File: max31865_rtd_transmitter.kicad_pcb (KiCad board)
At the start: 2 copper layers, 11 parts, among them CN1 WJ15EDGRM-3.81-4P-14-00A, SW1 MST22D18G2, T1 VPT87BB-01B, U1 MAX31865xTP, U2 VPS8504B, U3 TPS7A2033PDBVR, U4 TPS7A2033PDBVR, U5 ISO7741DWR

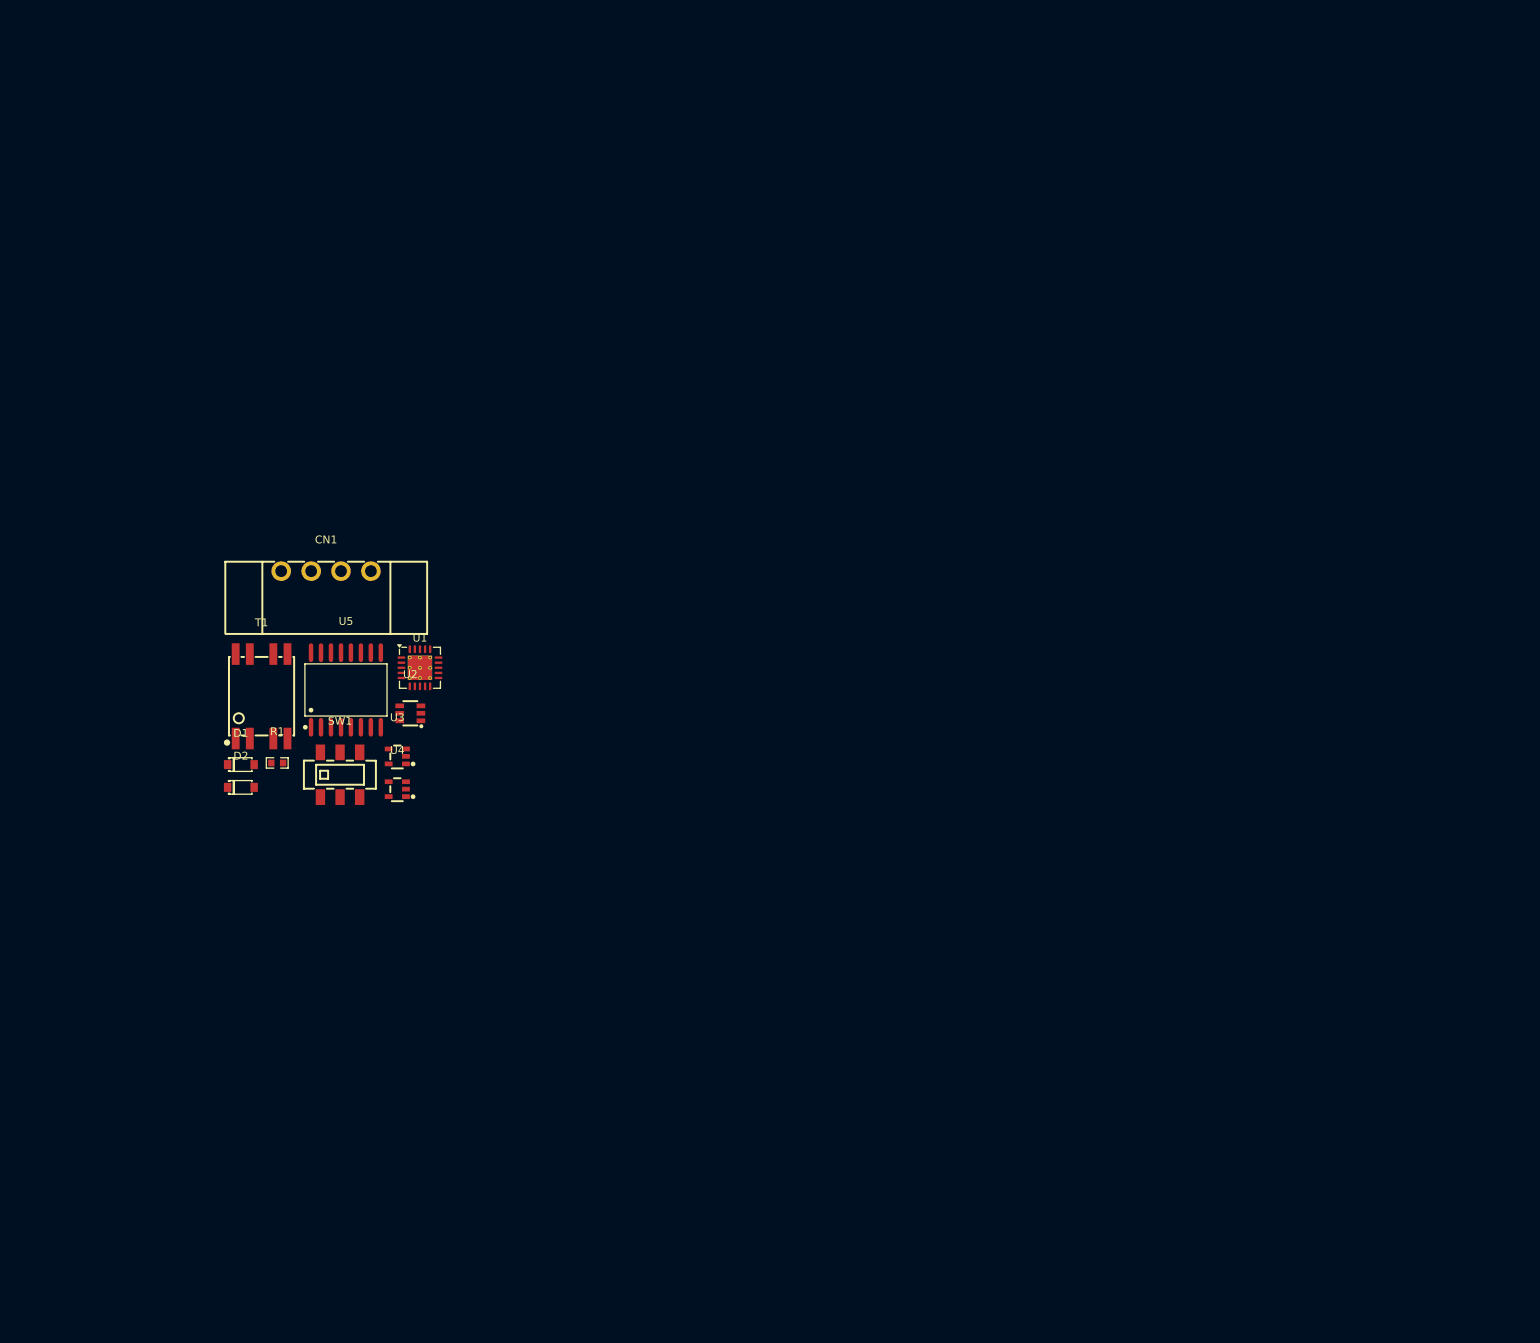
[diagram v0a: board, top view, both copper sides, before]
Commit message: Complete max31865 power supply and analog component layout
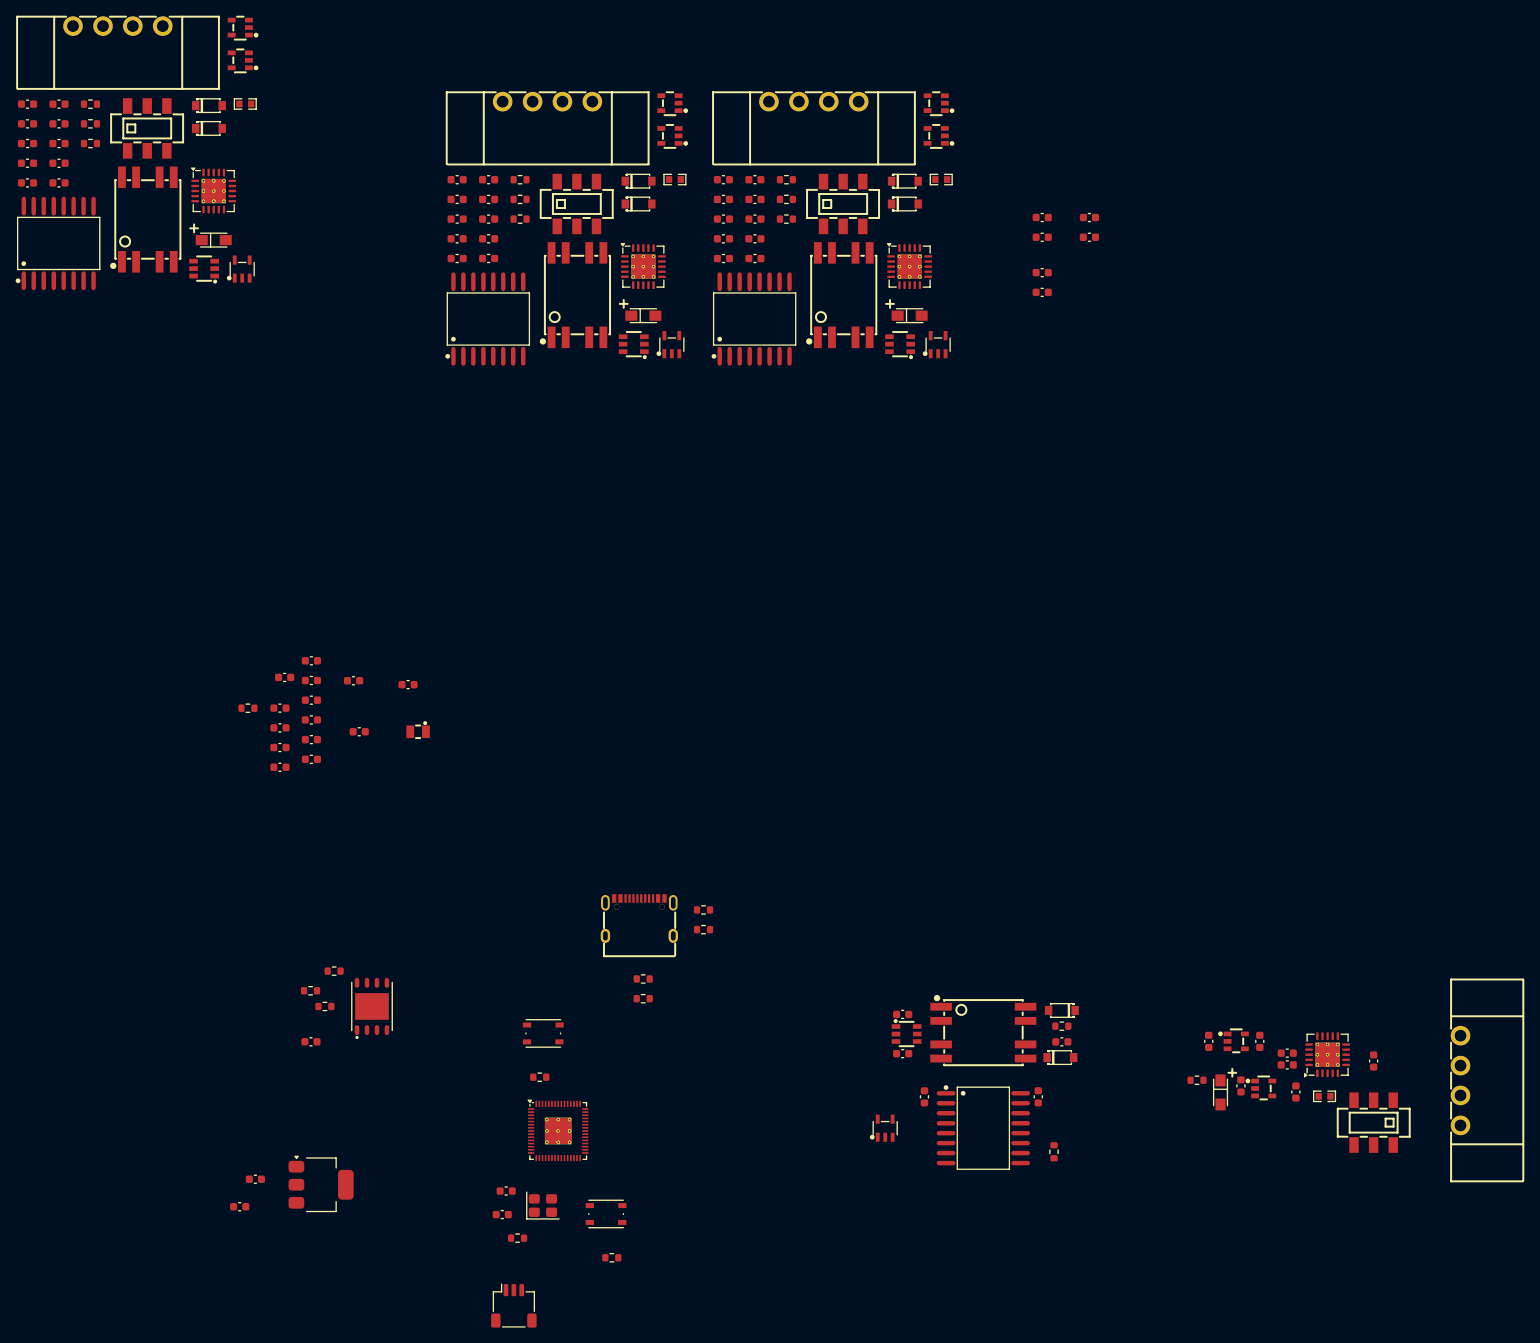
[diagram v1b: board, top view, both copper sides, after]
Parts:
- added C1: 15p, Capacitor_SMD:C_0603_1608Metric, F.Cu at (62.2, 98.5)
- added C10: 4.7u, Capacitor_SMD:C_0603_1608Metric, F.Cu at (33.4, 42.0)
- added C11: 100n, Capacitor_SMD:C_0603_1608Metric, F.Cu at (33.4, 44.5)
- added C12: 100n, Capacitor_SMD:C_0603_1608Metric, F.Cu at (34.0, 33.1)
- added C13: 100n, Capacitor_SMD:C_0603_1608Metric, F.Cu at (37.4, 31.0)
- added C14: 100n, Capacitor_SMD:C_0603_1608Metric, F.Cu at (37.4, 33.5)
- added C15: 100n, Capacitor_SMD:C_0603_1608Metric, F.Cu at (37.4, 36.0)
- added C16: 100n, Capacitor_SMD:C_0603_1608Metric, F.Cu at (37.4, 38.5)
- added C17: 100n, Capacitor_SMD:C_0603_1608Metric, F.Cu at (37.4, 41.0)
- added C18: 100n, Capacitor_SMD:C_0603_1608Metric, F.Cu at (37.4, 43.5)
- added C19: 10u, Capacitor_SMD:C_0603_1608Metric, F.Cu at (49.7, 34.0)
- added C2: 15p, Capacitor_SMD:C_0603_1608Metric, F.Cu at (61.7, 101.5)
- added C20: 100n, Capacitor_SMD:C_0603_1608Metric, F.Cu at (112.7, 81.0)
- added C21: 10u, Capacitor_SMD:C_0603_1608Metric, F.Cu at (112.7, 76.0)
- added C22: 4.7u, Capacitor_SMD:C_0603_1608Metric, F.Cu at (133.0, 79.5)
- added C23: 100n, Capacitor_SMD:C_0603_1608Metric, F.Cu at (161.7, 80.9)
- added C24: 100n, Capacitor_SMD:C_0603_1608Metric, F.Cu at (161.7, 82.4)
- added C25: 1u, Capacitor_SMD:C_0603_1608Metric, F.Cu at (151.7, 79.4)
- added C26: TAJA106K016RNJ, rtd-transmitter-library:CAP-SMD_L3.2-W1.6-RD-C7171, F.Cu at (153.2, 85.9)
- added C27: 10n, Capacitor_SMD:C_0603_1608Metric, F.Cu at (172.7, 81.9)
- added C28: 1u, Capacitor_SMD:C_0603_1608Metric, F.Cu at (155.8, 85.1)
- added C29: 1u, Capacitor_SMD:C_0603_1608Metric, F.Cu at (158.2, 79.4)
- added C3: 10u, Capacitor_SMD:C_0603_1608Metric, F.Cu at (30.3, 97.0)
- added C30: 1u, Capacitor_SMD:C_0603_1608Metric, F.Cu at (162.8, 85.9)
- added C31: 100n, Capacitor_SMD:C_0603_1608Metric, F.Cu at (1.25, -39.9)
- added C32: 10u, Capacitor_SMD:C_0603_1608Metric, F.Cu at (1.25, -37.4)
- added C33: 4.7u, Capacitor_SMD:C_0603_1608Metric, F.Cu at (1.25, -34.9)
- added C34: 100n, Capacitor_SMD:C_0603_1608Metric, F.Cu at (1.25, -32.4)
- added C35: 100n, Capacitor_SMD:C_0603_1608Metric, F.Cu at (1.25, -29.9)
- added C36: 1u, Capacitor_SMD:C_0603_1608Metric, F.Cu at (5.26, -39.9)
- added C37: TAJA106K016RNJ, rtd-transmitter-library:CAP-SMD_L3.2-W1.6-RD-C7171, F.Cu at (25.0, -22.6)
- added C38: 10n, Capacitor_SMD:C_0603_1608Metric, F.Cu at (5.26, -37.4)
- added C39: 1u, Capacitor_SMD:C_0603_1608Metric, F.Cu at (5.26, -34.9)
- added C4: 100n, Capacitor_SMD:C_0603_1608Metric, F.Cu at (37.4, 79.5)
- added C40: 1u, Capacitor_SMD:C_0603_1608Metric, F.Cu at (5.26, -32.4)
- added C41: 1u, Capacitor_SMD:C_0603_1608Metric, F.Cu at (5.26, -29.9)
- added C42: 100n, Capacitor_SMD:C_0603_1608Metric, F.Cu at (89.9, -30.3)
- added C43: 10u, Capacitor_SMD:C_0603_1608Metric, F.Cu at (89.9, -27.8)
- added C44: 4.7u, Capacitor_SMD:C_0603_1608Metric, F.Cu at (89.9, -25.3)
- added C45: 100n, Capacitor_SMD:C_0603_1608Metric, F.Cu at (89.9, -22.8)
- added C46: 100n, Capacitor_SMD:C_0603_1608Metric, F.Cu at (89.9, -20.3)
- added C47: 1u, Capacitor_SMD:C_0603_1608Metric, F.Cu at (93.9, -30.3)
- added C48: TAJA106K016RNJ, rtd-transmitter-library:CAP-SMD_L3.2-W1.6-RD-C7171, F.Cu at (113.6, -13.0)
- added C49: 10n, Capacitor_SMD:C_0603_1608Metric, F.Cu at (93.9, -27.8)
- added C5: 10u, Capacitor_SMD:C_0603_1608Metric, F.Cu at (28.3, 100.5)
- added C50: 1u, Capacitor_SMD:C_0603_1608Metric, F.Cu at (93.9, -25.3)
- added C51: 1u, Capacitor_SMD:C_0603_1608Metric, F.Cu at (93.9, -22.8)
- added C52: 1u, Capacitor_SMD:C_0603_1608Metric, F.Cu at (93.9, -20.3)
- added C53: 100n, Capacitor_SMD:C_0603_1608Metric, F.Cu at (56.0, -30.3)
- added C54: 10u, Capacitor_SMD:C_0603_1608Metric, F.Cu at (56.0, -27.8)
- added C55: 4.7u, Capacitor_SMD:C_0603_1608Metric, F.Cu at (56.0, -25.3)
- added C56: 100n, Capacitor_SMD:C_0603_1608Metric, F.Cu at (56.0, -22.8)
- added C57: 100n, Capacitor_SMD:C_0603_1608Metric, F.Cu at (56.0, -20.3)
- added C58: 1u, Capacitor_SMD:C_0603_1608Metric, F.Cu at (60.0, -30.3)
- added C59: TAJA106K016RNJ, rtd-transmitter-library:CAP-SMD_L3.2-W1.6-RD-C7171, F.Cu at (79.7, -13.0)
- added C6: 4.7u, Capacitor_SMD:C_0603_1608Metric, F.Cu at (42.8, 33.5)
- added C60: 10n, Capacitor_SMD:C_0603_1608Metric, F.Cu at (60.0, -27.8)
- added C61: 1u, Capacitor_SMD:C_0603_1608Metric, F.Cu at (60.0, -25.3)
- added C62: 1u, Capacitor_SMD:C_0603_1608Metric, F.Cu at (60.0, -22.8)
- added C63: 1u, Capacitor_SMD:C_0603_1608Metric, F.Cu at (60.0, -20.3)
- added C64: 100n, Capacitor_SMD:C_0603_1608Metric, F.Cu at (115.5, 86.5)
- added C65: 100n, Capacitor_SMD:C_0603_1608Metric, F.Cu at (136.5, -25.5)
- added C66: 100n, Capacitor_SMD:C_0603_1608Metric, F.Cu at (130.5, -18.5)
- added C67: 100n, Capacitor_SMD:C_0603_1608Metric, F.Cu at (130.5, -25.5)
- added C68: 100n, Capacitor_SMD:C_0603_1608Metric, F.Cu at (130.0, 86.5)
- added C69: 100n, Capacitor_SMD:C_0603_1608Metric, F.Cu at (136.5, -23.0)
- added C7: 4.7u, Capacitor_SMD:C_0603_1608Metric, F.Cu at (43.5, 40.0)
- added C70: 100n, Capacitor_SMD:C_0603_1608Metric, F.Cu at (130.5, -16.0)
- added C71: 100n, Capacitor_SMD:C_0603_1608Metric, F.Cu at (130.5, -23.0)
- added C8: 100n, Capacitor_SMD:C_0603_1608Metric, F.Cu at (33.4, 37.0)
- added C9: 4.7u, Capacitor_SMD:C_0603_1608Metric, F.Cu at (33.4, 39.5)
- added CN2: WJ15EDGRM-3.81-4P-14-00A, rtd-transmitter-library:CONN-TH_4P-P3.81_WJ15EDGRM-3.81-04P-14-00A, F.Cu at (12.8, -49.9)
- added CN3: WJ15EDGRM-3.81-4P-14-00A, rtd-transmitter-library:CONN-TH_4P-P3.81_WJ15EDGRM-3.81-04P-14-00A, F.Cu at (101.4, -40.3)
- added CN4: WJ15EDGRM-3.81-4P-14-00A, rtd-transmitter-library:CONN-TH_4P-P3.81_WJ15EDGRM-3.81-04P-14-00A, F.Cu at (67.5, -40.3)
- added D3: RB160M-30TR, rtd-transmitter-library:SOD-123_L2.8-W1.8-LS3.7-RD, F.Cu at (24.4, -39.8)
- added D4: RB160M-30TR, rtd-transmitter-library:SOD-123_L2.8-W1.8-LS3.7-RD, F.Cu at (24.4, -36.9)
- added D5: RB160M-30TR, rtd-transmitter-library:SOD-123_L2.8-W1.8-LS3.7-RD, F.Cu at (113.0, -30.1)
- added D6: RB160M-30TR, rtd-transmitter-library:SOD-123_L2.8-W1.8-LS3.7-RD, F.Cu at (113.0, -27.2)
- added D7: RB160M-30TR, rtd-transmitter-library:SOD-123_L2.8-W1.8-LS3.7-RD, F.Cu at (79.1, -30.1)
- added D8: RB160M-30TR, rtd-transmitter-library:SOD-123_L2.8-W1.8-LS3.7-RD, F.Cu at (79.1, -27.2)
- added J1: SM03B-SRSS-TB, Connector_JST:JST_SH_SM03B-SRSS-TB_1x03-1MP_P1.00mm_Horizontal, F.Cu at (63.2, 113.1)
- added L1: AOTA-B201610S3R3-101-T, rtd-transmitter-library:IND-SMD_L2.0-W1.6_AOTA-B201610S3R3-101-T, F.Cu at (51.0, 40.0)
- added R10: 27, Resistor_SMD:R_0603_1608Metric, F.Cu at (79.7, 71.5)
- added R11: 27, Resistor_SMD:R_0603_1608Metric, F.Cu at (79.7, 74.0)
- added R12: 47k, Resistor_SMD:R_0603_1608Metric, F.Cu at (132.0, 93.5)
- added R13: 4.7k, Resistor_SMD:R_0603_1608Metric, F.Cu at (133.0, 77.5)
- added R14: 2.2, Resistor_SMD:R_0603_1608Metric, F.Cu at (150.2, 84.4)
- added R15: PTFR0603B4K30P9, rtd-transmitter-library:R0603, F.Cu at (166.5, 86.4)
- added R16: 47k, Resistor_SMD:R_0603_1608Metric, F.Cu at (9.27, -39.9)
- added R17: 4.7k, Resistor_SMD:R_0603_1608Metric, F.Cu at (9.27, -37.4)
- added R18: 2.2, Resistor_SMD:R_0603_1608Metric, F.Cu at (9.27, -34.9)
- added R19: PTFR0603B4K30P9, rtd-transmitter-library:R0603, F.Cu at (29.0, -40.0)
- added R2: 0, Resistor_SMD:R_0603_1608Metric, F.Cu at (39.1, 75.0)
- added R20: 47k, Resistor_SMD:R_0603_1608Metric, F.Cu at (97.9, -30.3)
- added R21: 4.7k, Resistor_SMD:R_0603_1608Metric, F.Cu at (97.9, -27.8)
- added R22: 2.2, Resistor_SMD:R_0603_1608Metric, F.Cu at (97.9, -25.3)
- added R23: PTFR0603B4K30P9, rtd-transmitter-library:R0603, F.Cu at (117.6, -30.3)
- added R24: 47k, Resistor_SMD:R_0603_1608Metric, F.Cu at (64.0, -30.3)
- added R25: 4.7k, Resistor_SMD:R_0603_1608Metric, F.Cu at (64.0, -27.8)
- added R26: 2.2, Resistor_SMD:R_0603_1608Metric, F.Cu at (64.0, -25.3)
- added R27: PTFR0603B4K30P9, rtd-transmitter-library:R0603, F.Cu at (83.7, -30.3)
- added R3: DNF, Resistor_SMD:R_0603_1608Metric, F.Cu at (40.3, 70.5)
- added R4: 5.1k, Resistor_SMD:R_0603_1608Metric, F.Cu at (87.4, 62.7)
- added R5: 5.1k, Resistor_SMD:R_0603_1608Metric, F.Cu at (87.4, 65.2)
- added R6: 1k, Resistor_SMD:R_0603_1608Metric, F.Cu at (63.7, 104.5)
- added R7: 1k, Resistor_SMD:R_0603_1608Metric, F.Cu at (75.7, 107.0)
- added R8: 33, Resistor_SMD:R_0603_1608Metric, F.Cu at (29.3, 37.0)
- added R9: 1k, Resistor_SMD:R_0603_1608Metric, F.Cu at (66.5, 84.0)
- added SW2: SW_Push, Button_Switch_SMD:SW_Push_1P1T_NO_Vertical_Wuerth_434133025816, F.Cu at (75.0, 101.4)
- added SW3: MST22D18G2, rtd-transmitter-library:SW-SMD_MST22D18G2, F.Cu at (172.7, 89.8)
- added SW4: MST22D18G2, rtd-transmitter-library:SW-SMD_MST22D18G2, F.Cu at (16.5, -36.9)
- added SW5: MST22D18G2, rtd-transmitter-library:SW-SMD_MST22D18G2, F.Cu at (105.1, -27.2)
- added SW6: MST22D18G2, rtd-transmitter-library:SW-SMD_MST22D18G2, F.Cu at (71.2, -27.2)
- added T2: VPT87BB-01B, rtd-transmitter-library:XFMR-SMD_VPSC_VPT87BB, F.Cu at (16.6, -25.2)
- added T3: VPT87BB-01B, rtd-transmitter-library:XFMR-SMD_VPSC_VPT87BB, F.Cu at (105.2, -15.6)
- added T4: VPT87BB-01B, rtd-transmitter-library:XFMR-SMD_VPSC_VPT87BB, F.Cu at (71.3, -15.6)
- added U10: VPS8504B, rtd-transmitter-library:SOT-23-6_L2.9-W1.6-P0.95-LS2.8-BR, F.Cu at (23.7, -19.0)
- added U11: SN74LVC1G125DBVR, rtd-transmitter-library:SOT-23-5_L3.0-W1.7-P0.95-LS2.8-BL, F.Cu at (28.6, -18.9)
- added U12: ISO7741DWR, rtd-transmitter-library:SOIC-16_L10.3-W7.5-P1.27-LS10.3-BL, F.Cu at (5.22, -22.2)
- added U13: MAX31865xTP, Package_DFN_QFN:TQFN-20-1EP_5x5mm_P0.65mm_EP3.1x3.1mm_ThermalVias, F.Cu at (25.0, -28.9)
- added U14: TPS7A2033PDBVR, rtd-transmitter-library:SOT-23-5_L2.9-W1.6-P0.95-LS2.8-BR, F.Cu at (28.4, -49.7)
- added U15: TPS7A2033PDBVR, rtd-transmitter-library:SOT-23-5_L2.9-W1.6-P0.95-LS2.8-BR, F.Cu at (28.4, -45.5)
- added U16: VPS8504B, rtd-transmitter-library:SOT-23-6_L2.9-W1.6-P0.95-LS2.8-BR, F.Cu at (112.4, -9.37)
- added U17: SN74LVC1G125DBVR, rtd-transmitter-library:SOT-23-5_L3.0-W1.7-P0.95-LS2.8-BL, F.Cu at (117.2, -9.30)
- added U18: ISO7741DWR, rtd-transmitter-library:SOIC-16_L10.3-W7.5-P1.27-LS10.3-BL, F.Cu at (93.9, -12.6)
- added U19: MAX31865xTP, Package_DFN_QFN:TQFN-20-1EP_5x5mm_P0.65mm_EP3.1x3.1mm_ThermalVias, F.Cu at (113.6, -19.2)
- added U20: TPS7A2033PDBVR, rtd-transmitter-library:SOT-23-5_L2.9-W1.6-P0.95-LS2.8-BR, F.Cu at (117.0, -40.1)
- added U21: TPS7A2033PDBVR, rtd-transmitter-library:SOT-23-5_L2.9-W1.6-P0.95-LS2.8-BR, F.Cu at (117.0, -35.9)
- added U22: VPS8504B, rtd-transmitter-library:SOT-23-6_L2.9-W1.6-P0.95-LS2.8-BR, F.Cu at (78.5, -9.37)
- added U23: SN74LVC1G125DBVR, rtd-transmitter-library:SOT-23-5_L3.0-W1.7-P0.95-LS2.8-BL, F.Cu at (83.3, -9.30)
- added U24: ISO7741DWR, rtd-transmitter-library:SOIC-16_L10.3-W7.5-P1.27-LS10.3-BL, F.Cu at (60.0, -12.6)
- added U25: MAX31865xTP, Package_DFN_QFN:TQFN-20-1EP_5x5mm_P0.65mm_EP3.1x3.1mm_ThermalVias, F.Cu at (79.7, -19.2)
- added U26: TPS7A2033PDBVR, rtd-transmitter-library:SOT-23-5_L2.9-W1.6-P0.95-LS2.8-BR, F.Cu at (83.1, -40.1)
- added U27: TPS7A2033PDBVR, rtd-transmitter-library:SOT-23-5_L2.9-W1.6-P0.95-LS2.8-BR, F.Cu at (83.1, -35.9)
- added U6: ISO7741DWR, rtd-transmitter-library:SOIC-16_L10.3-W7.5-P1.27-LS10.3-BL, F.Cu at (123.0, 90.5)
- added U7: MAX31865xTP, Package_DFN_QFN:TQFN-20-1EP_5x5mm_P0.65mm_EP3.1x3.1mm_ThermalVias, F.Cu at (166.8, 81.1)
- added U8: TPS7A2033PDBVR, rtd-transmitter-library:SOT-23-5_L2.9-W1.6-P0.95-LS2.8-BR, F.Cu at (155.2, 79.4)
- added U9: TPS7A2033PDBVR, rtd-transmitter-library:SOT-23-5_L2.9-W1.6-P0.95-LS2.8-BR, F.Cu at (158.7, 85.4)
- added USB1: TYPE-C 16PIN 2MD(073), rtd-transmitter-library:USB-C-SMD_TYPE-C-6PIN-2MD-073, F.Cu at (79.2, 63.6)
- added Y1: ABM8-272-T3, Crystal:Crystal_SMD_3225-4Pin_3.2x2.5mm, F.Cu at (66.9, 100.3)
- R1: value PTFR0603B4K30P9 -> DNF; footprint rtd-transmitter-library:R0603 -> Resistor_SMD:R_0603_1608Metric
- SW1: value MST22D18G2 -> SW_Push; footprint rtd-transmitter-library:SW-SMD_MST22D18G2 -> Button_Switch_SMD:SW_Push_1P1T_NO_Vertical_Wuerth_434133025816
- U1: value MAX31865xTP -> W25Q32JVZPIQ; footprint Package_DFN_QFN:TQFN-20-1EP_5x5mm_P0.65mm_EP3.1x3.1mm_ThermalVias -> rtd-transmitter-library:WSON-8_L6.0-W5.0-P1.27-BL-EP
- U2: value VPS8504B -> NCP1117-3.3_SOT223; footprint rtd-transmitter-library:SOT-23-6_L2.9-W1.6-P0.95-LS2.8-BR -> Package_TO_SOT_SMD:SOT-223-3_TabPin2
- U3: value TPS7A2033PDBVR -> RP2350_60QFN; footprint rtd-transmitter-library:SOT-23-5_L2.9-W1.6-P0.95-LS2.8-BR -> Package_DFN_QFN:QFN-60-1EP_7x7mm_P0.4mm_EP3.4x3.4mm_ThermalVias
- U4: value TPS7A2033PDBVR -> VPS8504B; footprint rtd-transmitter-library:SOT-23-5_L2.9-W1.6-P0.95-LS2.8-BR -> rtd-transmitter-library:SOT-23-6_L2.9-W1.6-P0.95-LS2.8-BR
- U5: value ISO7741DWR -> SN74LVC1G125DBVR; footprint rtd-transmitter-library:SOIC-16_L10.3-W7.5-P1.27-LS10.3-BL -> rtd-transmitter-library:SOT-23-5_L3.0-W1.7-P0.95-LS2.8-BL
- moved CN1 158.4 mm to (183.8, 84.4), turned to 90 degrees
- moved D2 109.9 mm to (132.8, 81.5)
- moved D1 109.2 mm to (133.0, 75.5), turned to 180 degrees
- moved T1 101.4 mm to (123.0, 78.3), turned to -90 degrees
- moved U5 88.5 mm to (110.5, 90.5)
- moved U4 72.0 mm to (113.2, 78.5), turned to 180 degrees
- moved U2 61.1 mm to (38.6, 97.7)
- moved U3 51.9 mm to (68.8, 90.8)
- moved U1 43.6 mm to (45.1, 75.0)
- moved SW1 41.9 mm to (67.0, 78.4)
- moved R1 29.3 mm to (37.3, 73.0)
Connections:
- CN1 pad 2: Net-(U1-RTDIN+) -> Net-(U7-RTDIN+)
- CN1 pad 3: Net-(U1-RTDIN-) -> Net-(U7-RTDIN-)
- CN1 pad 4: Net-(U1-FORCE-) -> Net-(U7-FORCE-)
- D1 pad 1: Net-(U3-EN) -> /31865_ch0/V_trans
- D2 pad 1: Net-(U3-EN) -> /31865_ch0/V_trans
- R1 pad 1: Net-(U1-ISENSOR) -> /rp2350/GPIO0
- R1 pad 2: Net-(U1-BIAS) -> /rp2350/FLASH_SS
- SW1 pad 1: unconnected-(SW1-Pad1) -> GND
- SW1 pad 2: unconnected-(SW1-Pad2) -> /rp2350/~{USB_BOOT}
- T1 pad 1: Net-(U2-VD1) -> Net-(U4-VD1)
- T1 pad 4: Net-(U2-VD2) -> Net-(U4-VD2)
- U1 pad 1: Net-(U1-BIAS) -> /rp2350/FLASH_SS
- U1 pad 2: Net-(U1-BIAS) -> /rp2350/QSPI_SD1
- U1 pad 3: Net-(U1-ISENSOR) -> /rp2350/QSPI_SD2
- U1 pad 4: Net-(U1-ISENSOR) -> GND
- U1 pad 5: /31865_ch0/force+ -> /rp2350/QSPI_SD0
- U1 pad 6: /31865_ch0/force2 -> /rp2350/QSPI_SCLK
- U1 pad 7: Net-(U1-RTDIN+) -> /rp2350/QSPI_SD3
- U1 pad 8: Net-(U1-RTDIN-) -> +3V3
- U1 pad 9: Net-(U1-FORCE-) -> GND
- U2 pad 1: +5V -> GND
- U2 pad 2: GND -> +3V3
- U2 pad 3: unconnected-(U2-CLK-Pad3) -> VBUS
- U3 pad 1: Net-(U3-EN) -> +3V3
- U3 pad 2: /31865_ch0/local_gnd -> /rp2350/GPIO0
- U3 pad 3: Net-(U3-EN) -> /rp2350/GPIO1
- U3 pad 4: unconnected-(U3-NC-Pad4) -> /rp2350/GPIO2
- U3 pad 5: /31865_ch0/local_3v3_digital -> /rp2350/GPIO3
- U4 pad 1: Net-(U3-EN) -> +5V
- U4 pad 2: /31865_ch0/local_gnd -> GND
- U4 pad 3: Net-(U3-EN) -> unconnected-(U4-CLK-Pad3)
- U4 pad 4: unconnected-(U4-NC-Pad4) -> Net-(U4-VD2)
- U4 pad 5: /31865_ch0/local_3v3_analog -> +5V
- U5 pad 1: +5V -> /rp2350/GPIO5
- U5 pad 2: GND1 -> /31865_ch0/CH_SDO_LOWZ
- U5 pad 3: /31865_ch0/CH_SDI -> GND
- U5 pad 4: /31865_ch0/CH_SCLK -> /rp2350/GPIO4
- U5 pad 5: /31865_ch0/CH_~{CS} -> +5V

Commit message: start pcb layout, add sd card and screen
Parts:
- moved C13 72.4 mm to (74.4, 93.2)
- moved C12 68.6 mm to (74.4, 88.6)
- moved C8 67.7 mm to (64.7, 97.0), turned to 180 degrees
- moved C14 67.7 mm to (64.7, 95.4), turned to 180 degrees
- moved R8 67.3 mm to (77.7, 83.8)
- moved C15 67.3 mm to (67.2, 96.3), turned to -90 degrees
- moved C9 63.7 mm to (62.4, 96.2), turned to -90 degrees
- moved C11 62.0 mm to (74.4, 91.0)
- moved L1 60.7 mm to (65.8, 98.9)
- moved C16 59.5 mm to (60.0, 93.5), turned to 180 degrees
- moved C17 58.5 mm to (60.0, 95.0), turned to 180 degrees
- moved C6 57.7 mm to (59.9, 88.6), turned to 180 degrees
- moved C19 54.3 mm to (77.6, 80.6)
- moved C10 53.3 mm to (67.1, 83.3), turned to 90 degrees
- moved C7 52.8 mm to (59.9, 90.2), turned to 180 degrees
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
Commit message: Complete single channel design
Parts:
- removed CN1, CN2, CN3, CN4: WJ15EDGRM-3.81-4P-14-00A, rtd-transmitter-library:CONN-TH_4P-P3.81_WJ15EDGRM-3.81-04P-14-00A
- added C72: 10u, Capacitor_SMD:C_0603_1608Metric, F.Cu at (93.0, 127.5)
- added C73: 10u, Capacitor_SMD:C_0603_1608Metric, F.Cu at (93.0, 130.0)
- added C74: 10u, Capacitor_SMD:C_0603_1608Metric, F.Cu at (93.0, 132.5)
- added C75: 100n, Capacitor_SMD:C_0603_1608Metric, F.Cu at (93.0, 135.0)
- added CN5: WJ15EDGRC-3.81-4P, rtd-transmitter-library:CONN-TH_WJ15EDGRC-3.81-4P, F.Cu at (133.9, 48.5)
- added CN6: WJ15EDGRC-3.81-4P, rtd-transmitter-library:CONN-TH_WJ15EDGRC-3.81-4P, F.Cu at (156.5, 48.4)
- added CN7: WJ15EDGRC-3.81-4P, rtd-transmitter-library:CONN-TH_WJ15EDGRC-3.81-4P, F.Cu at (179.2, 48.4)
- added CN8: WJ15EDGRC-3.81-4P, rtd-transmitter-library:CONN-TH_WJ15EDGRC-3.81-4P, F.Cu at (201.4, 48.4)
- added Card1: TF-01A, rtd-transmitter-library:TF-SMD_TF-01A, F.Cu at (82.2, 132.7)
- added SW7: OS4D501110, rtd-transmitter-library:SW-SMD_L6.0-W6.0-P6.00-LS6.8, F.Cu at (78.9, 176.9)
- added U28: HS20HS072RX, rtd-transmitter-library:OLED-SMD_HS20HS072RX, F.Cu at (48.3, 196.9)
- added U29: NCP1117-3.3_SOT223, Package_TO_SOT_SMD:SOT-223-3_TabPin2, F.Cu at (78.2, 147.1)
- added U30: LGS63042, rtd-transmitter-library:SOT-23-5_L2.9-W1.6-P0.95-LS2.8-BL, F.Cu at (69.3, 128.3)
- SW3, SW4, SW5, SW6: moved to B.Cu
- moved C31 213.5 mm to (153.2, 110.0), turned to -90 degrees
- moved C32 207.7 mm to (147.6, 109.9), turned to -90 degrees
- moved R16 203.2 mm to (164.6, 91.1)
- moved C53 199.8 mm to (198.2, 110.0), turned to -90 degrees
- moved U12 197.3 mm to (161.1, 98.8)
- moved C33 194.8 mm to (151.7, 88.9), turned to -90 degrees
- moved C54 193.9 mm to (192.5, 109.9), turned to -90 degrees
- moved R24 189.5 mm to (209.5, 91.1)
- moved C39 189.4 mm to (157.3, 78.1)
- moved R17 188.9 mm to (149.7, 88.9), turned to -90 degrees
- moved C36 188.2 mm to (152.6, 77.2)
- moved R18 187.8 mm to (153.9, 84.8), turned to 90 degrees
- moved U11 185.0 mm to (162.0, 109.3), turned to 180 degrees
- moved C35 184.9 mm to (157.8, 68.4), turned to -90 degrees
- moved C34 184.4 mm to (155.7, 68.4), turned to -90 degrees
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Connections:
- C23 pad 2: /31865_ch0/local_gnd_analog -> /31865_ch0/local_3v3_digital
- C30 pad 2: /31865_ch0/local_gnd_analog -> /31865_ch0/local_gnd
- C34 pad 2: /31865_ch1/local_gnd_analog -> /31865_ch1/local_3v3_digital
- C41 pad 2: /31865_ch1/local_gnd_analog -> /31865_ch1/local_gnd
- C45 pad 2: /31865_ch2/local_gnd_analog -> /31865_ch2/local_3v3_digital
- C52 pad 2: /31865_ch2/local_gnd_analog -> /31865_ch2/local_gnd
- C56 pad 2: /31865_ch3/local_gnd_analog -> /31865_ch3/local_3v3_digital
- C63 pad 2: /31865_ch3/local_gnd_analog -> /31865_ch3/local_gnd
- SW3 pad 1: unconnected-(SW3-Pad1) -> /31865_ch0/local_gnd_analog
- SW3 pad 2: unconnected-(SW3-Pad2) -> /31865_ch0/force2
- SW3 pad 3: unconnected-(SW3-Pad3) -> /31865_ch0/force+
- SW3 pad 4: GND -> unconnected-(SW3-Pad4)
- SW3 pad 5: /31865_ch0/force2 -> unconnected-(SW3-Pad5)
- SW3 pad 6: /31865_ch0/force+ -> unconnected-(SW3-Pad6)
- SW4 pad 1: unconnected-(SW4-Pad1) -> /31865_ch1/local_gnd_analog
- SW4 pad 2: unconnected-(SW4-Pad2) -> /31865_ch1/force2
- SW4 pad 3: unconnected-(SW4-Pad3) -> /31865_ch1/force+
- SW4 pad 4: GND -> unconnected-(SW4-Pad4)
- SW4 pad 5: /31865_ch1/force2 -> unconnected-(SW4-Pad5)
- SW4 pad 6: /31865_ch1/force+ -> unconnected-(SW4-Pad6)
- SW5 pad 1: unconnected-(SW5-Pad1) -> /31865_ch2/local_gnd_analog
- SW5 pad 2: unconnected-(SW5-Pad2) -> /31865_ch2/force2
- SW5 pad 3: unconnected-(SW5-Pad3) -> /31865_ch2/force+
- SW5 pad 4: GND -> unconnected-(SW5-Pad4)
- SW5 pad 5: /31865_ch2/force2 -> unconnected-(SW5-Pad5)
- SW5 pad 6: /31865_ch2/force+ -> unconnected-(SW5-Pad6)
- SW6 pad 1: unconnected-(SW6-Pad1) -> /31865_ch3/local_gnd_analog
- SW6 pad 2: unconnected-(SW6-Pad2) -> /31865_ch3/force2
- SW6 pad 3: unconnected-(SW6-Pad3) -> /31865_ch3/force+
- SW6 pad 4: GND -> unconnected-(SW6-Pad4)
- SW6 pad 5: /31865_ch3/force2 -> unconnected-(SW6-Pad5)
- SW6 pad 6: /31865_ch3/force+ -> unconnected-(SW6-Pad6)
- USB1 pad 13: unconnected-(USB1-SHELL-Pad13) -> Earth
- USB1 pad 14: unconnected-(USB1-SHELL-Pad14) -> Earth
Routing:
- net +5V: track 0.00 -> 61.5 mm, vias 0 -> 36
- net /31865_ch0/local_3v3_digital: track 0.00 -> 40.6 mm, vias 0 -> 8
- net /31865_ch3/local_3v3_digital: track 0.00 -> 40.6 mm, vias 0 -> 8
- net /31865_ch1/local_3v3_digital: track 0.00 -> 40.6 mm, vias 0 -> 8
- net /31865_ch2/local_3v3_digital: track 0.00 -> 40.6 mm, vias 0 -> 8
- net Net-(U18-OUTA): track 0.00 -> 38.2 mm, vias 0 -> 2
- net Net-(U6-OUTA): track 0.00 -> 38.2 mm, vias 0 -> 2
- net Net-(U12-OUTA): track 0.00 -> 38.2 mm, vias 0 -> 2
- net Net-(U24-OUTA): track 0.00 -> 38.2 mm, vias 0 -> 2
- net Net-(U6-OUTB): track 0.00 -> 37.1 mm, vias 0 -> 2
- net Net-(U18-OUTB): track 0.00 -> 37.1 mm, vias 0 -> 2
- net Net-(U12-OUTB): track 0.00 -> 37.1 mm, vias 0 -> 2
- net Net-(U24-OUTB): track 0.00 -> 37.1 mm, vias 0 -> 2
- net Net-(U6-IND): track 0.00 -> 36.7 mm, vias 0 -> 2
- net Net-(U18-IND): track 0.00 -> 36.7 mm, vias 0 -> 2
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- added copper zone on F.Cu, net +5V
- added copper zone on F.Cu, net /31865_ch0/local_gnd
- added copper zone on F.Cu, net /31865_ch1/local_gnd
- added copper zone on F.Cu, net /31865_ch2/local_gnd
- added copper zone on F.Cu, net /31865_ch3/local_gnd
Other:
- copper layers 2 -> 4
- board text added: "20260323: Connect trace to switch and connector"
